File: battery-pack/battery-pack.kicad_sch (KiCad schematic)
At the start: 1 part, among them J1 USB_C_Receptacle

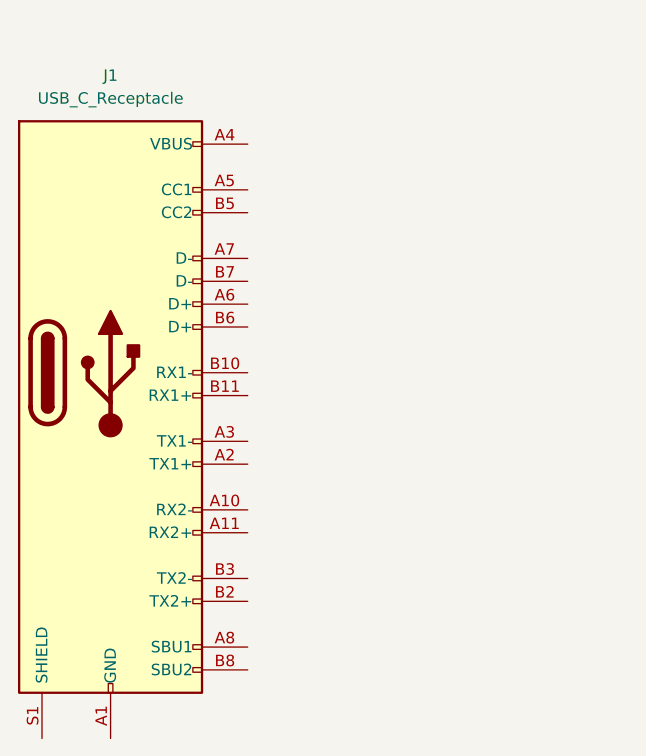
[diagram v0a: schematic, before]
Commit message: Update battery-pack.kicad_sch
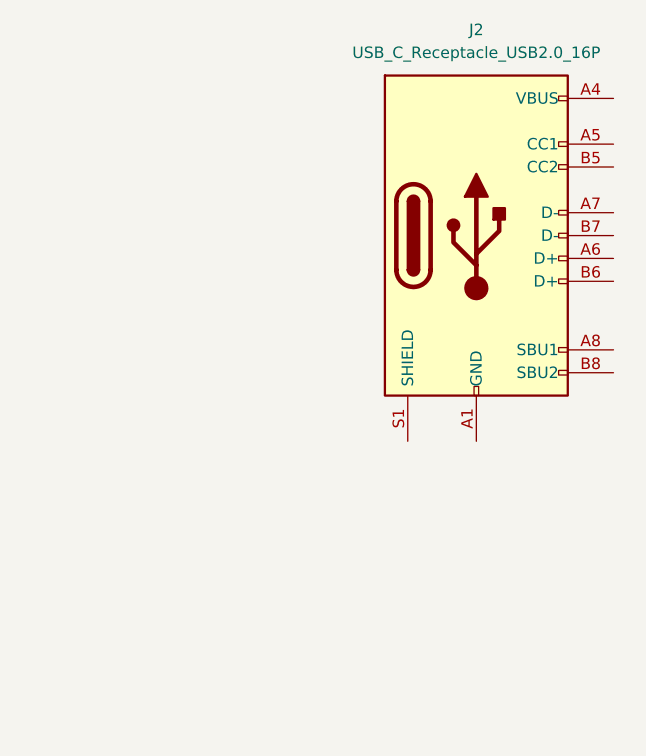
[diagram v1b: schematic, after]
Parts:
- removed J1: USB_C_Receptacle, Connector_USB:USB_C_Receptacle_Molex_105450-0101, symbol Connector:USB_C_Receptacle
- added J2: USB_C_Receptacle_USB2.0_16P, Connector_USB:USB_C_Receptacle_G-Switch_GT-USB-7010ASV, symbol Connector:USB_C_Receptacle_USB2.0_16P
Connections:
- new net: J2.A1 (GND), J2.A12 (GND), J2.B1 (GND), J2.B12 (GND)
- new net: J2.A4 (VBUS), J2.A9 (VBUS), J2.B4 (VBUS), J2.B9 (VBUS)
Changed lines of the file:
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@@
 	(paper "A4")
 	(symbol
-		(lib_id "Connector:USB_C_Receptacle")
-		(at 60.96 76.2 0)
+		(lib_id "Connector:USB_C_Receptacle_USB2.0_16P")
+		(at 101.6 60.96 0)
 		(unit 1)
 		(exclude_from_sim no)
@@
 		(dnp no)
 		(fields_autoplaced yes)
-		(property "Reference" "J1"
-			(at 60.96 43.18 0)
+		(property "Reference" "J2"
+			(at 101.6 38.1 0)
 			(effects
 				(font
@@
 			)
 		)
-		(property "Value" "USB_C_Receptacle"
-			(at 60.96 45.72 0)
+		(property "Value" "USB_C_Receptacle_USB2.0_16P"
+			(at 101.6 40.64 0)
 			(effects
 				(font
@@
 			)
 		)
-		(property "Footprint" "Connector_USB:USB_C_Receptacle_Molex_105450-0101"
-			(at 64.77 76.2 0)
+		(property "Footprint" "Connector_USB:USB_C_Receptacle_G-Switch_GT-USB-7010ASV"
+			(at 105.41 60.96 0)
 			(effects
 				(font
@@
 		)
 		(property "Datasheet" "https://www.usb.org/sites/default/files/documents/usb_type-c.zip"
-			(at 64.77 76.2 0)
+			(at 105.41 60.96 0)
 			(effects
 				(font
@@
 			)
 		)
-		(property "Description" "USB Full-Featured Type-C Receptacle connector"
-			(at 60.96 76.2 0)
+		(property "Description" "USB 2.0-only 16P Type-C Receptacle connector"
+			(at 101.6 60.96 0)
 			(effects
 				(font
@@
 			)
 		)
-		(pin "B12"
-		)
-		(pin "B6"
-		)
-		(pin "B8"
-		)
-		(pin "A4"
-		)
-		(pin "A9"
-		)
-		(pin "A1"
-		)
-		(pin "A10"
-		)
-		(pin "A11"
-		)
-		(pin "A12"
-		)
-		(pin "A7"
-		)
-		(pin "B10"
-		)
-		(pin "B11"
-		)
-		(pin "A8"
-		)
-		(pin "A2"
-		)
-		(pin "A3"
-		)
-		(pin "A6"
-		)
-		(pin "A5"
-		)
-		(pin "B1"
-		)
-		(pin "B2"
-		)
-		(pin "B3"
-		)
-		(pin "B4"
-		)
-		(pin "B5"
-		)
 		(pin "B7"
 		)
@@
 		(pin "S1"
 		)
+		(pin "B12"
+		)
+		(pin "A6"
+		)
+		(pin "B6"
+		)
+		(pin "A5"
+		)
+		(pin "A4"
+		)
+		(pin "B8"
+		)
+		(pin "A7"
+		)
+		(pin "A1"
+		)
+		(pin "A9"
+		)
+		(pin "A12"
+		)
+		(pin "B5"
+		)
+		(pin "B1"
+		)
+		(pin "B4"
+		)
+		(pin "A8"
+		)
 		(instances
 			(project "battery-pack"
 				(path "/027043dd-9aea-494a-9ac9-d75fab205bcb"
-					(reference "J1")
+					(reference "J2")
 					(unit 1)
 				)

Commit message: work
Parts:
- removed J2: USB_C_Receptacle_USB2.0_16P, Connector_USB:USB_C_Receptacle_G-Switch_GT-USB-7010ASV, symbol Connector:USB_C_Receptacle_USB2.0_16P
- added J1, J3: USB_C_Receptacle_USB2.0_16P, Connector_USB:USB_C_Receptacle_G-Switch_GT-USB-7010ASV, symbol Connector:USB_C_Receptacle_USB2.0_16P
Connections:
- new net: J1.A1 (GND), J1.A12 (GND), J1.B1 (GND), J1.B12 (GND)
- new net: J1.A4 (VBUS), J1.A9 (VBUS), J1.B4 (VBUS), J1.B9 (VBUS)
- new net: J3.A1 (GND), J3.A12 (GND), J3.B1 (GND), J3.B12 (GND)
- new net: J3.A4 (VBUS), J3.A9 (VBUS), J3.B4 (VBUS), J3.B9 (VBUS)
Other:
- added sheet Port1 (port.kicad_sch)
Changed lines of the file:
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@@
 (kicad_sch
-	(version 20231120)
+	(version 20250114)
 	(generator "eeschema")
-	(generator_version "8.0")
+	(generator_version "9.0")
 	(paper "A4")
 	(symbol
 		(lib_id "Connector:USB_C_Receptacle_USB2.0_16P")
-		(at 101.6 60.96 0)
+		(at 231.14 93.98 0)
+		(mirror y)
 		(unit 1)
 		(exclude_from_sim no)
@@
 		(on_board yes)
 		(dnp no)
-		(fields_autoplaced yes)
-		(property "Reference" "J2"
-			(at 101.6 38.1 0)
+		(property "Reference" "J1"
+			(at 231.14 71.12 0)
 			(effects
 				(font
@@
 		)
 		(property "Value" "USB_C_Receptacle_USB2.0_16P"
-			(at 101.6 40.64 0)
+			(at 231.14 73.66 0)
 			(effects
 				(font
@@
 		)
 		(property "Footprint" "Connector_USB:USB_C_Receptacle_G-Switch_GT-USB-7010ASV"
-			(at 105.41 60.96 0)
+			(at 227.33 93.98 0)
 			(effects
 				(font
@@
 		)
 		(property "Datasheet" "https://www.usb.org/sites/default/files/documents/usb_type-c.zip"
-			(at 105.41 60.96 0)
+			(at 227.33 93.98 0)
 			(effects
 				(font
@@
 		)
 		(property "Description" "USB 2.0-only 16P Type-C Receptacle connector"
-			(at 101.6 60.96 0)
+			(at 231.14 93.98 0)
 			(effects
 				(font
@@
 			(project "battery-pack"
 				(path "/027043dd-9aea-494a-9ac9-d75fab205bcb"
-					(reference "J2")
+					(reference "J1")
 					(unit 1)
+				)
+			)
+		)
+	)
+	(symbol
+		(lib_id "Connector:USB_C_Receptacle_USB2.0_16P")
+		(at 231.14 144.78 0)
+		(mirror y)
+		(unit 1)
+		(exclude_from_sim no)
+		(in_bom yes)
+		(on_board yes)
+		(dnp no)
+		(property "Reference" "J3"
+			(at 231.14 121.92 0)
+			(effects
+				(font
+					(size 1.27 1.27)
+				)
+			)
+		)
+		(property "Value" "USB_C_Receptacle_USB2.0_16P"
+			(at 231.14 124.46 0)
+			(effects
+				(font
+					(size 1.27 1.27)
+				)
+			)
+		)
+		(property "Footprint" "Connector_USB:USB_C_Receptacle_G-Switch_GT-USB-7010ASV"
+			(at 227.33 144.78 0)
+			(effects
+				(font
+					(size 1.27 1.27)
+				)
+				(hide yes)
+			)
+		)
+		(property "Datasheet" "https://www.usb.org/sites/default/files/documents/usb_type-c.zip"
+			(at 227.33 144.78 0)
+			(effects
+				(font
+					(size 1.27 1.27)
+				)
+				(hide yes)
+			)
+		)
+		(property "Description" "USB 2.0-only 16P Type-C Receptacle connector"
+			(at 231.14 144.78 0)
+			(effects
+				(font
+					(size 1.27 1.27)
+				)
+				(hide yes)
+			)
+		)
+		(pin "B7"
+		)
+		(pin "B9"
+		)
+		(pin "S1"
+		)
+		(pin "B12"
+		)
+		(pin "A6"
+		)
+		(pin "B6"
+		)
+		(pin "A5"
+		)
+		(pin "A4"
+		)
+		(pin "B8"
+		)
+		(pin "A7"
+		)
+		(pin "A1"
+		)
+		(pin "A9"
+		)
+		(pin "A12"
+		)
+		(pin "B5"
+		)
+		(pin "B1"
+		)
+		(pin "B4"
+		)
+		(pin "A8"
+		)
+		(instances
+			(project "battery-pack"
+				(path "/027043dd-9aea-494a-9ac9-d75fab205bcb"
+					(reference "J3")
+					(unit 1)
+				)
+			)
+		)
+	)
+	(sheet
+		(at 81.28 127)
+		(size 67.31 33.02)
+		(exclude_from_sim no)
+		(in_bom yes)
+		(on_board yes)
+		(dnp no)
+		(fields_autoplaced yes)
+		(stroke
+			(width 0.1524)
+			(type solid)
+		)
+		(fill
+			(color 0 0 0 0.0000)
+		)
+		(property "Sheetname" "Port1"
+			(at 81.28 126.2884 0)
+			(effects
+				(font
+					(size 1.27 1.27)
+				)
+				(justify left bottom)
+			)
+		)
+		(property "Sheetfile" "port.kicad_sch"
+			(at 81.28 160.6046 0)
+			(effects
+				(font
+					(size 1.27 1.27)
+				)
+				(justify left top)
+			)
+		)
+		(instances
+			(project "battery-pack"
+				(path "/027043dd-9aea-494a-9ac9-d75fab205bcb"
+					(page "2")
 				)
 			)
@@
 		)
 	)
+	(embedded_fonts no)
 )
